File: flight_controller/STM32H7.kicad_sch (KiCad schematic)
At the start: 65 parts, among them SW1 6.0*6.0*6.0, U1 HB-PH9-12727PB2GOB, U2 STM32H743IIT6, X1 XKXEL89CLI-SUAYLC-32.768K, X2 XL2EL89CLI-111YLC-16M

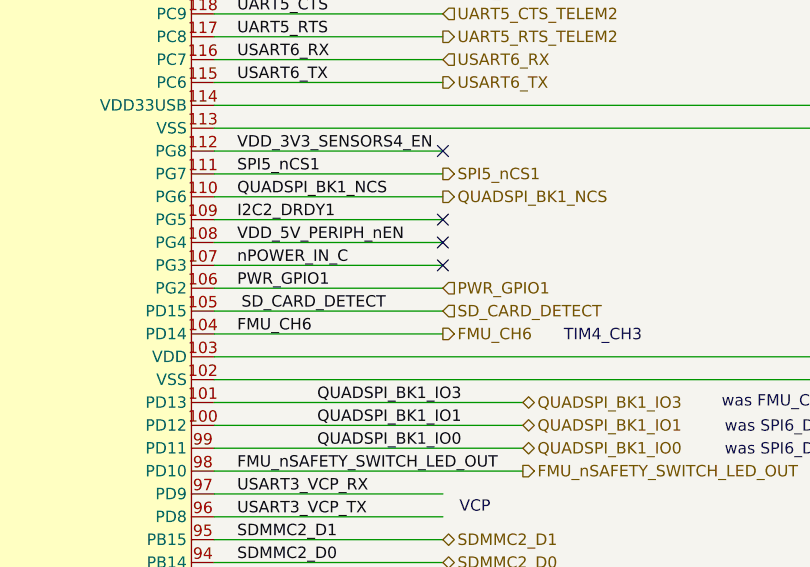
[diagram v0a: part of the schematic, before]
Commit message: Updated power and usb connectors and netlist check
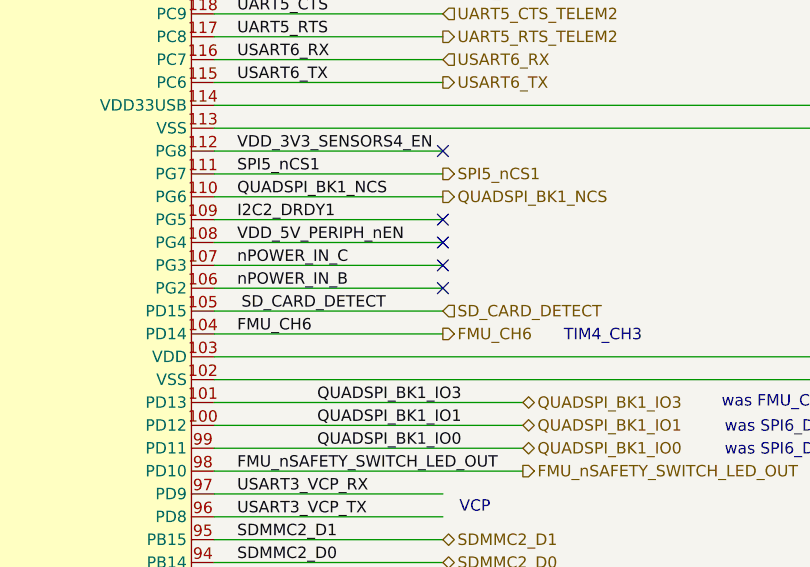
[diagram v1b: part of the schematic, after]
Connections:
- net PWR_GPIO1 renamed nPOWER_IN_B
- no-connect marks 35 -> 36
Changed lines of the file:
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@@
 	)
 	(no_connect
+		(at 511.81 186.69)
+	)
+	(no_connect
 		(at 364.49 270.51)
 	)
@@
 			(width 0)
 			(type default)
+			(color 255 0 0 1)
 		)
 	)
@@
 		)
 	)
-	(label "PWR_GPIO1"
+	(label "nPOWER_IN_B"
 		(at 488.95 186.69 0)
 		(effects
@@
 		)
 	)
-	(hierarchical_label "PWR_GPIO1"
-		(shape input)
-		(at 511.81 186.69 0)
-		(effects
-			(font
-				(size 1.27 1.27)
-			)
-			(justify left)
-		)
-	)
